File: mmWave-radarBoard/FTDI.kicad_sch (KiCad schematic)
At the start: 39 parts, among them U301 FT4232H, U302 93LCxxB

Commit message: Updated schematic
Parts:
- removed NT203, NT204, NT205: NetTie_2, symbol Device:NetTie_2
- added C284, C285: 8pF, symbol Device:C
- added FB301, FB302, FB303: 600@100MHz 0.3A, symbol Device:FerriteBead
- added Y102: 12MHz, Crystal:Crystal_SMD_2016-4Pin_2.0x1.6mm, symbol Device:Crystal_GND24
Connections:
- net FTDI_3V3: now also FB301.2, FB302.1, FB303.1
- net FTDI_SPI_CLK: now also R230.2, U301.16 (ADBUS0)
- net FTDI_SPI_CS: now also R233.2, U301.19 (ADBUS3)
- net FTDI_SPI_MISO: now also R232.2, U301.18 (ADBUS2)
- net FTDI_SPI_MOSI: now also R231.2, U301.17 (ADBUS1)
- net GND: now also C284.2, C285.2, Y102.2, Y102.4
- net VCC_3V3: now also FB301.1
- net VPHY_FTDI: now also FB303.2
- net VPLL_FTDI: now also FB302.2
- net ~{FTDI_SUSPEND}: now reaches R243.1, R244.2
- net FTDI_HOST_INT_1: now reaches R237.1
- net FTDI_HOST_INT_1: now also R238.1
- net HOSTIRQ_FTDI_IN: now reaches R237.2, U301.32 (BDBUS5)
- net RST_FTDI: now reaches R236.1, U301.14 (~{RESET})
- net XTAL_M: now reaches U301.2 (OSCI)
- net XTAL_M: now also C284.1, Y102.1
- net XTAL_P: now reaches U301.3 (OSCO)
- net XTAL_P: now also C285.1, Y102.3
- net HOSTIRQ_FTDI_OUT: now reaches R238.2, U301.34 (BDBUS7)
- net ~{RST}_FTDI: now reaches R239.2, U301.45 (CDBUS6)
- net SOP1_FTDI: now reaches R240.2, U301.54 (DDBUS3)
- net SOP0_FTDI: now reaches R241.2, U301.55 (DDBUS4)
- net REF_FTDI: now reaches R235.1, U301.6 (REF)
- net FTDI_USBD+: now reaches U301.7 (DM)
- net FTDI_USBD-: now reaches U301.8 (DP)
- net FTDI_SOP0: now reaches R241.1
- net USER_LED_WS_GPIO_0: now reaches R242.1
- net RADAR_~{RST}_2: now reaches R239.1
- net FTDI_SOP1: now reaches R240.1
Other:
- company: Emiel V -> Designer: EV
- moved on the sheet: C264, C265, C266, C267, C268, C269, C270, C271, C272, C273, C274, C275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

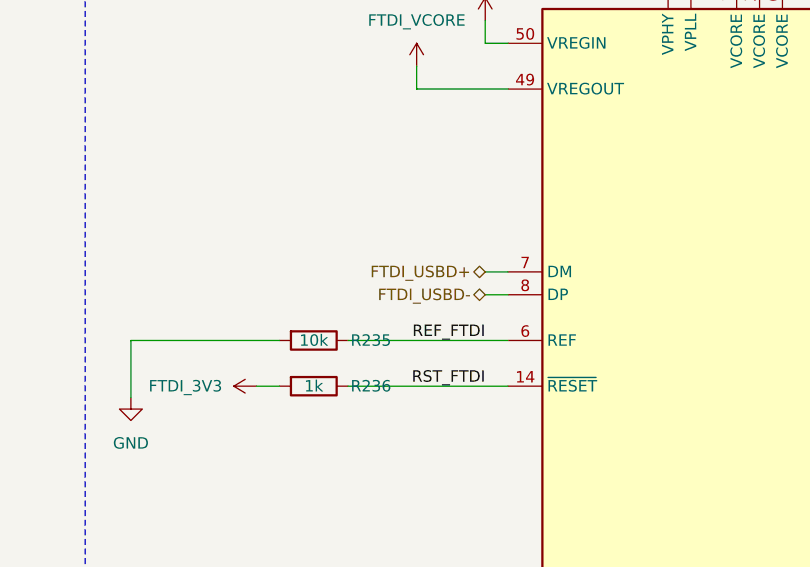
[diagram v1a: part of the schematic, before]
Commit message: Updated schematic of the radar module
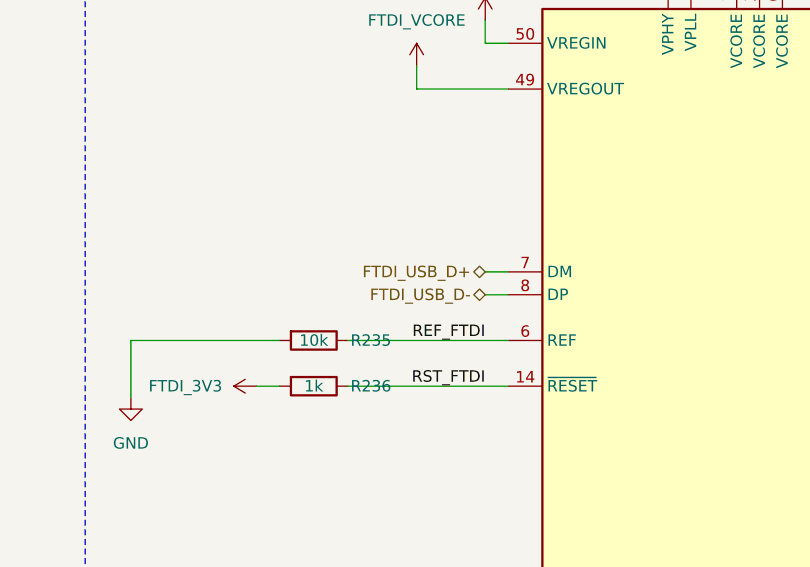
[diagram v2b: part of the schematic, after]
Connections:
- net FTDI_USBD+ renamed FTDI_USB_D+
- net FTDI_USBD- renamed FTDI_USB_D-
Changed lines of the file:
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@@
 		)
 	)
-	(hierarchical_label "FTDI_USBD+"
+	(hierarchical_label "FTDI_USB_D+"
 		(shape bidirectional)
 		(at 179.07 118.11 180)
@@
 		)
 	)
-	(hierarchical_label "FTDI_USBD-"
+	(hierarchical_label "FTDI_USB_D-"
 		(shape bidirectional)
 		(at 179.07 120.65 180)

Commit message: Removed unnecessary bits
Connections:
- net USR_LED_SW: now also R242.2, U301.59 (DDBUS7)
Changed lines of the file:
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@@
 	)
 	(label "USR_LED_SW"
-		(at 243.84 181.61 0)
+		(at 243.84 179.07 0)
 		(effects
 			(font

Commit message: Finished schematic
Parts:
- C301: renamed from C266; footprint (none) -> Capacitor_SMD:C_0402_1005Metric
- C302: renamed from C265; footprint (none) -> Capacitor_SMD:C_0402_1005Metric
- C303: renamed from C276; footprint (none) -> Capacitor_SMD:C_0402_1005Metric
- C304: renamed from C277; footprint (none) -> Capacitor_SMD:C_0402_1005Metric
- C305: renamed from C264; footprint (none) -> Capacitor_SMD:C_0603_1608Metric
- C306: renamed from C267; footprint (none) -> Capacitor_SMD:C_0402_1005Metric
- C307: renamed from C268; footprint (none) -> Capacitor_SMD:C_0402_1005Metric
- C308: renamed from C274; footprint (none) -> Capacitor_SMD:C_0402_1005Metric
- C309: renamed from C275; footprint (none) -> Capacitor_SMD:C_0402_1005Metric
- C310: renamed from C269; footprint (none) -> Capacitor_SMD:C_0402_1005Metric
- C311: renamed from C270; footprint (none) -> Capacitor_SMD:C_0402_1005Metric
- C312: renamed from C273; footprint (none) -> Capacitor_SMD:C_0402_1005Metric
- C313: renamed from C272; footprint (none) -> Capacitor_SMD:C_0402_1005Metric
- C314: renamed from C271; footprint (none) -> Capacitor_SMD:C_0402_1005Metric
- C315: renamed from C284; footprint (none) -> Capacitor_SMD:C_0402_1005Metric
- C316: renamed from C285; footprint (none) -> Capacitor_SMD:C_0402_1005Metric
- D301: renamed from D207; footprint (none) -> LED_SMD:LED_0603_1608Metric
- FB301: footprint (none) -> Inductor_SMD:L_0603_1608Metric
- FB302: renamed from FB303; footprint (none) -> Inductor_SMD:L_0603_1608Metric
- FB303: renamed from FB302; footprint (none) -> Inductor_SMD:L_0603_1608Metric
- R301: renamed from R234; footprint (none) -> Resistor_SMD:R_0402_1005Metric
- R302: renamed from R230; footprint (none) -> Resistor_SMD:R_0402_1005Metric
- R303: renamed from R231; footprint (none) -> Resistor_SMD:R_0402_1005Metric
- R304: renamed from R232; footprint (none) -> Resistor_SMD:R_0402_1005Metric
- R305: renamed from R233; footprint (none) -> Resistor_SMD:R_0402_1005Metric
- R306: renamed from R235; footprint (none) -> Resistor_SMD:R_0402_1005Metric
- R307: renamed from R237; footprint (none) -> Resistor_SMD:R_0402_1005Metric
- R308: renamed from R227; footprint (none) -> Resistor_SMD:R_0402_1005Metric
- R309: renamed from R228; footprint (none) -> Resistor_SMD:R_0402_1005Metric
- R310: renamed from R236; footprint (none) -> Resistor_SMD:R_0402_1005Metric
- R311: renamed from R229; footprint (none) -> Resistor_SMD:R_0402_1005Metric
- R312: renamed from R238; footprint (none) -> Resistor_SMD:R_0402_1005Metric
- R313: renamed from R226; footprint (none) -> Resistor_SMD:R_0402_1005Metric
- R314: renamed from R239; footprint (none) -> Resistor_SMD:R_0402_1005Metric
- R315: renamed from R240; footprint (none) -> Resistor_SMD:R_0402_1005Metric; now fitted
- R316: renamed from R241; footprint (none) -> Resistor_SMD:R_0402_1005Metric; now fitted
- R317: renamed from R242; footprint (none) -> Resistor_SMD:R_0402_1005Metric; now fitted
- R318: renamed from R243; footprint (none) -> Resistor_SMD:R_0402_1005Metric
- R319: renamed from R244; footprint (none) -> Resistor_SMD:R_0603_1608Metric
- renumbered Y102 to Y301

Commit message: Updated radar PCB and schematic
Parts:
- removed U301: FT4232H, Package_QFP:LQFP-64_10x10mm_P0.5mm, symbol Interface_USB:FT4232H
- added U301: FT4232HQ, FT4232HQ:QFN50P900X900X105-65N, symbol FT4232HQ:FT4232HQ
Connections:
- net EECLK: now also U301.61 (EEDATA)
- net EECS: now also U301.63 (EECS)
- net EEDATA: now also U301.62 (EECLK)
- net FTDI_3V3: now also U301.20 (VCCIO), U301.31 (VCCIO), U301.42 (VCCIO), U301.50 (VREGIN), U301.56 (VCCIO)
- net FTDI_SPI_CLK: no longer R302.2
- net FTDI_SPI_CS: no longer R305.2
- net FTDI_SPI_MISO: no longer R304.2
- net FTDI_SPI_MOSI: no longer R303.2
- net FTDI_USB_D+: now also U301.7 (DM)
- net FTDI_USB_D-: now also U301.8 (DP)
- net FTDI_VCORE: now also U301.12 (VCORE), U301.37 (VCORE_), U301.49 (VREGOUT), U301.64 (VCORE)
- net GND: now also U301.1 (GND), U301.10 (AGND), U301.11 (GND), U301.13 (TEST), U301.15 (GND), U301.25 (GND), U301.35 (GND), U301.47 (GND), U301.5 (GND), U301.51 (GND), U301.65 (EXP)
- net HOSTIRQ_FTDI_IN: now also U301.32 (BDBUS5)
- net HOSTIRQ_FTDI_OUT: now also U301.34 (BDBUS7)
- net REF_FTDI: now also U301.6 (REF)
- net RST_FTDI: now also U301.14 (~{RESET})
- net SOP0_FTDI: now also U301.55 (DDBUS4)
- net SOP1_FTDI: now also U301.54 (DDBUS3)
- net USR_LED_SW: now also U301.59 (DDBUS7)
- net VPHY_FTDI: now also U301.4 (VPHY)
- net VPLL_FTDI: now also U301.9 (VPLL)
- net XTAL_M: now also U301.2 (OSCI)
- net XTAL_P: now also U301.3 (OSCO)
- net ~{RST}_FTDI: now also U301.45 (CDBUS6)
- net at R318.2: now also U301.36 (~{SUSPEND})
- new net SPI_CLK: R302.2, U301.16 (ADBUS0)
- new net SPI_CS: R305.2, U301.19 (ADBUS3)
- new net SPI_MISO: R304.2, U301.18 (ADBUS2)
- new net SPI_MOSI: R303.2, U301.17 (ADBUS1)
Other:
- moved on the sheet: D301, R301, R302, R303, R304, R305, R306, R307, R310, R312, R314, R315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

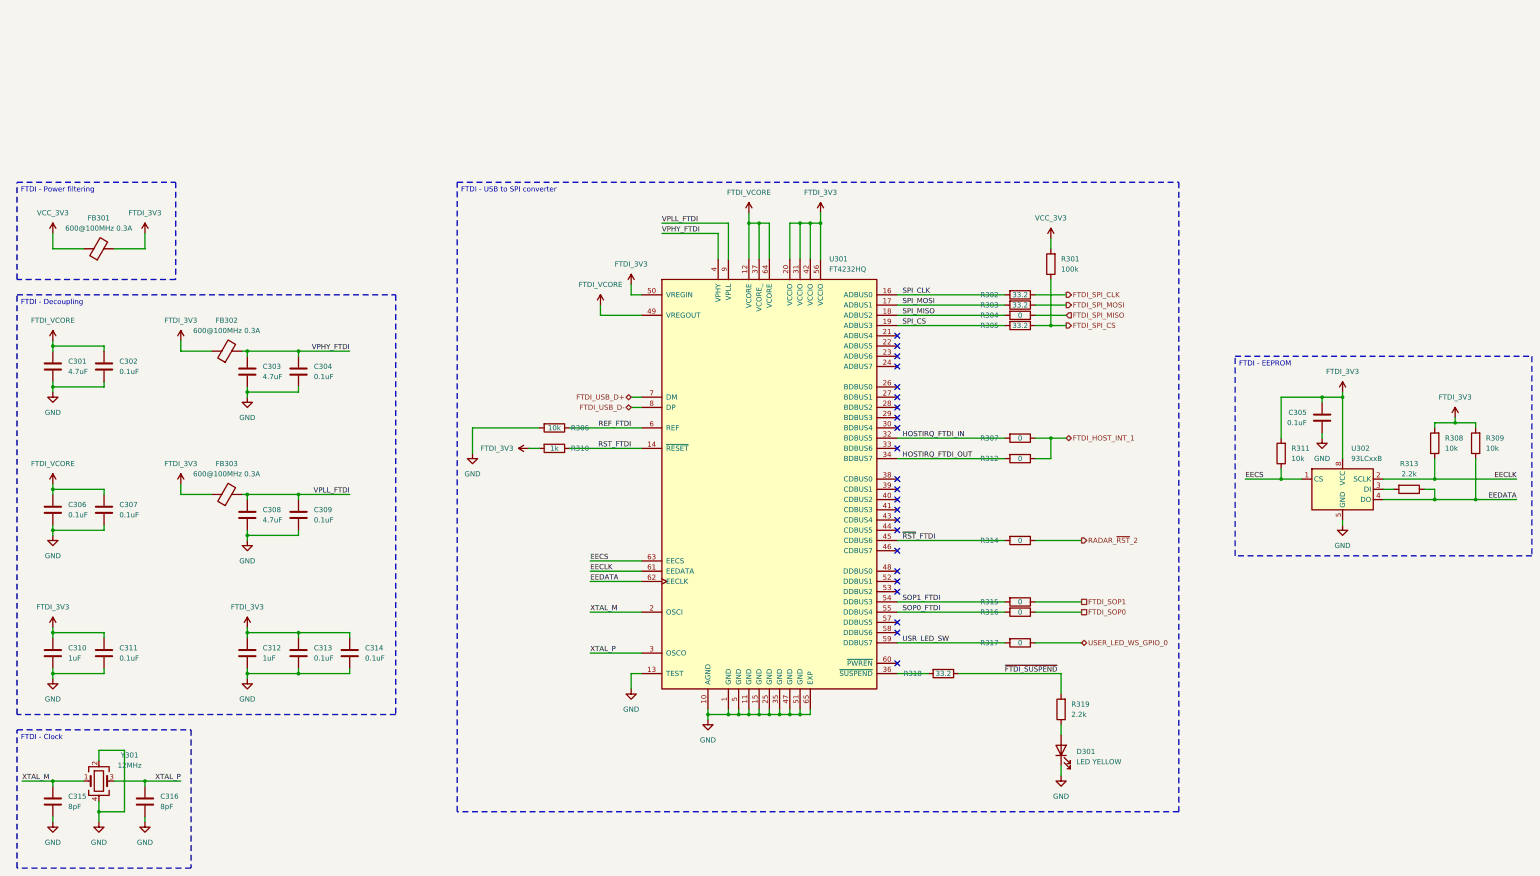
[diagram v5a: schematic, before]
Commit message: Updated schematic and PCB
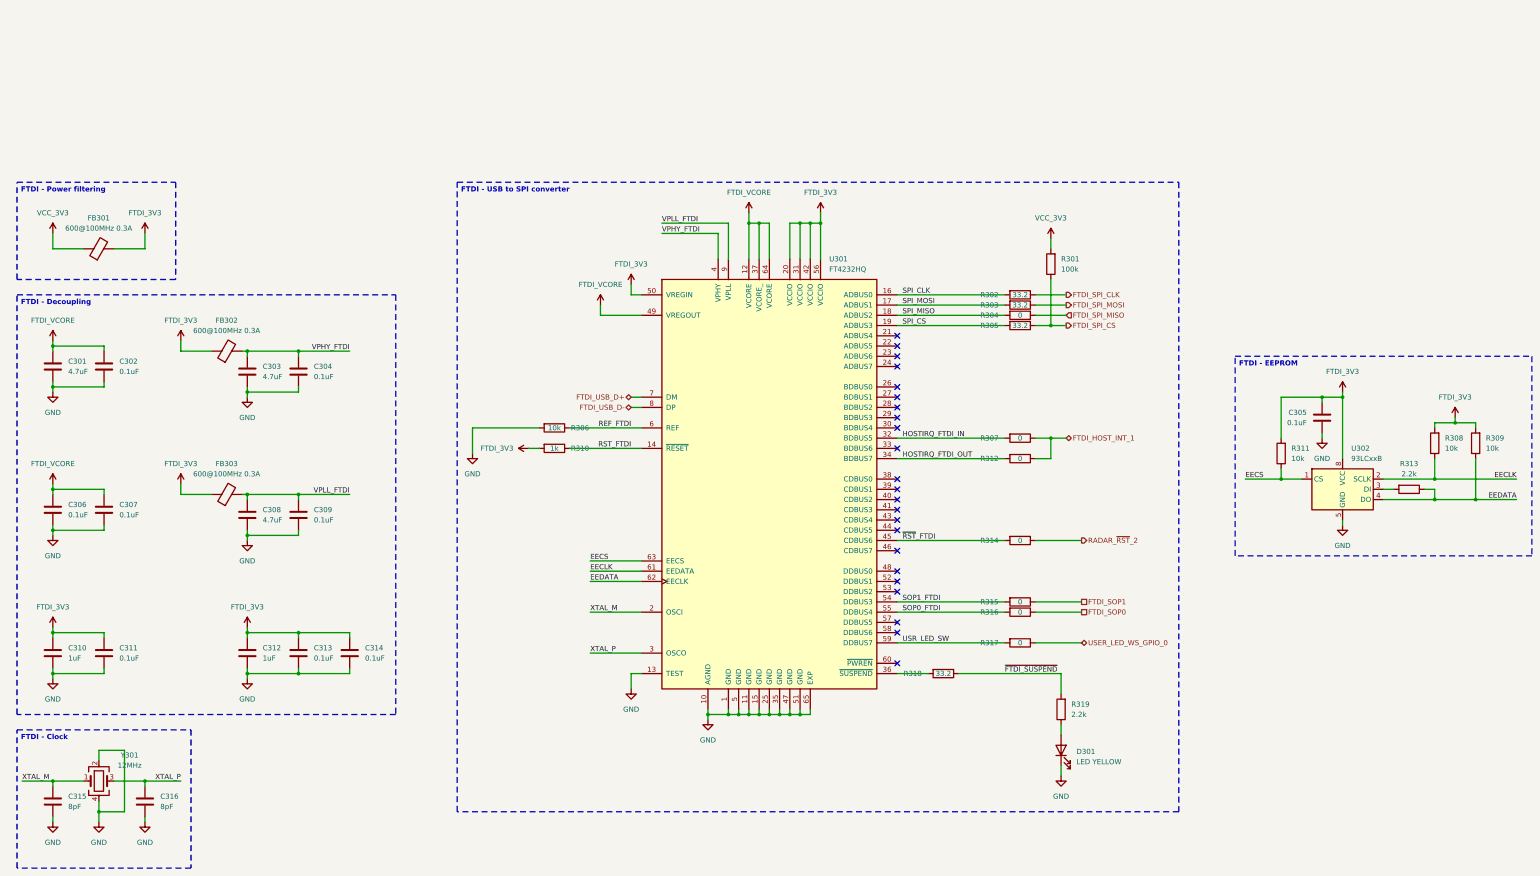
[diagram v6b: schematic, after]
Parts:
- C302, C304, C306, C307, C309, C311, C313, C314: footprint Capacitor_SMD:C_0402_1005Metric -> Capacitor_SMD:C_0201_0603Metric
- R301, R302, R303, R304, R305, R306, R307, R310, R312, R314, R315, R316, R317, R318: footprint Resistor_SMD:R_0402_1005Metric -> Resistor_SMD:R_0201_0603Metric

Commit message: Updated schematic and PCB
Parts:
- C302, C304, C306, C307, C309, C311, C313, C314: footprint Capacitor_SMD:C_0201_0603Metric -> Capacitor_SMD:C_0402_1005Metric
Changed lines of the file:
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@@
 			)
 		)
-		(property "Footprint" "Capacitor_SMD:C_0201_0603Metric"
+		(property "Footprint" "Capacitor_SMD:C_0402_1005Metric"
 			(at 96.2152 115.57 0)
 			(effects
@@
 			)
 		)
-		(property "Footprint" "Capacitor_SMD:C_0201_0603Metric"
+		(property "Footprint" "Capacitor_SMD:C_0402_1005Metric"
 			(at 47.9552 149.86 0)
 			(effects
@@
 			)
 		)
-		(property "Footprint" "Capacitor_SMD:C_0201_0603Metric"
+		(property "Footprint" "Capacitor_SMD:C_0402_1005Metric"
 			(at 96.2152 151.13 0)
 			(effects
@@
 			)
 		)
-		(property "Footprint" "Capacitor_SMD:C_0201_0603Metric"
+		(property "Footprint" "Capacitor_SMD:C_0402_1005Metric"
 			(at 35.2552 149.86 0)
 			(effects
@@
 			)
 		)
-		(property "Footprint" "Capacitor_SMD:C_0201_0603Metric"
+		(property "Footprint" "Capacitor_SMD:C_0402_1005Metric"
 			(at 47.9552 185.42 0)
 			(effects
@@
 			)
 		)
-		(property "Footprint" "Capacitor_SMD:C_0201_0603Metric"
+		(property "Footprint" "Capacitor_SMD:C_0402_1005Metric"
 			(at 96.2152 185.42 0)
 			(effects
@@
 			)
 		)
-		(property "Footprint" "Capacitor_SMD:C_0201_0603Metric"
+		(property "Footprint" "Capacitor_SMD:C_0402_1005Metric"
 			(at 108.9152 185.42 0)
 			(effects
@@
 			)
 		)
-		(property "Footprint" "Capacitor_SMD:C_0201_0603Metric"
+		(property "Footprint" "Capacitor_SMD:C_0402_1005Metric"
 			(at 47.9552 114.3 0)
 			(effects

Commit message: Updated PCB
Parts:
- R301, R302, R303, R304, R305, R306, R307, R310, R312, R314, R315, R316, R317, R318: footprint Resistor_SMD:R_0201_0603Metric -> Resistor_SMD:R_0402_1005Metric
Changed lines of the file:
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@@
 			)
 		)
-		(property "Footprint" "Resistor_SMD:R_0201_0603Metric"
+		(property "Footprint" "Resistor_SMD:R_0402_1005Metric"
 			(at 274.32 126.492 90)
 			(effects
@@
 			)
 		)
-		(property "Footprint" "Resistor_SMD:R_0201_0603Metric"
+		(property "Footprint" "Resistor_SMD:R_0402_1005Metric"
 			(at 158.75 129.032 90)
 			(effects
@@
 			)
 		)
-		(property "Footprint" "Resistor_SMD:R_0201_0603Metric"
+		(property "Footprint" "Resistor_SMD:R_0402_1005Metric"
 			(at 274.32 169.672 90)
 			(effects
@@
 			)
 		)
-		(property "Footprint" "Resistor_SMD:R_0201_0603Metric"
+		(property "Footprint" "Resistor_SMD:R_0402_1005Metric"
 			(at 274.32 93.472 90)
 			(effects
@@
 			)
 		)
-		(property "Footprint" "Resistor_SMD:R_0201_0603Metric"
+		(property "Footprint" "Resistor_SMD:R_0402_1005Metric"
 			(at 255.27 184.912 90)
 			(effects
@@
 			)
 		)
-		(property "Footprint" "Resistor_SMD:R_0201_0603Metric"
+		(property "Footprint" "Resistor_SMD:R_0402_1005Metric"
 			(at 274.32 177.292 90)
 			(effects
@@
 			)
 		)
-		(property "Footprint" "Resistor_SMD:R_0201_0603Metric"
+		(property "Footprint" "Resistor_SMD:R_0402_1005Metric"
 			(at 274.32 131.572 90)
 			(effects
@@
 			)
 		)
-		(property "Footprint" "Resistor_SMD:R_0201_0603Metric"
+		(property "Footprint" "Resistor_SMD:R_0402_1005Metric"
 			(at 283.718 85.09 90)
 			(effects
@@
 			)
 		)
-		(property "Footprint" "Resistor_SMD:R_0201_0603Metric"
+		(property "Footprint" "Resistor_SMD:R_0402_1005Metric"
 			(at 274.32 96.012 90)
 			(effects
@@
 			)
 		)
-		(property "Footprint" "Resistor_SMD:R_0201_0603Metric"
+		(property "Footprint" "Resistor_SMD:R_0402_1005Metric"
 			(at 274.32 98.552 90)
 			(effects
@@
 			)
 		)
-		(property "Footprint" "Resistor_SMD:R_0201_0603Metric"
+		(property "Footprint" "Resistor_SMD:R_0402_1005Metric"
 			(at 274.32 151.892 90)
 			(effects
@@
 			)
 		)
-		(property "Footprint" "Resistor_SMD:R_0201_0603Metric"
+		(property "Footprint" "Resistor_SMD:R_0402_1005Metric"
 			(at 274.32 90.932 90)
 			(effects
@@
 			)
 		)
-		(property "Footprint" "Resistor_SMD:R_0201_0603Metric"
+		(property "Footprint" "Resistor_SMD:R_0402_1005Metric"
 			(at 274.32 167.132 90)
 			(effects
@@
 			)
 		)
-		(property "Footprint" "Resistor_SMD:R_0201_0603Metric"
+		(property "Footprint" "Resistor_SMD:R_0402_1005Metric"
 			(at 158.75 123.952 90)
 			(effects
